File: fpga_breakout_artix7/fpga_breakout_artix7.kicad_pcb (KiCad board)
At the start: 4 copper layers, 26.4 x 25.4 mm, 41 parts, among them U1 XC7A15TCPG236

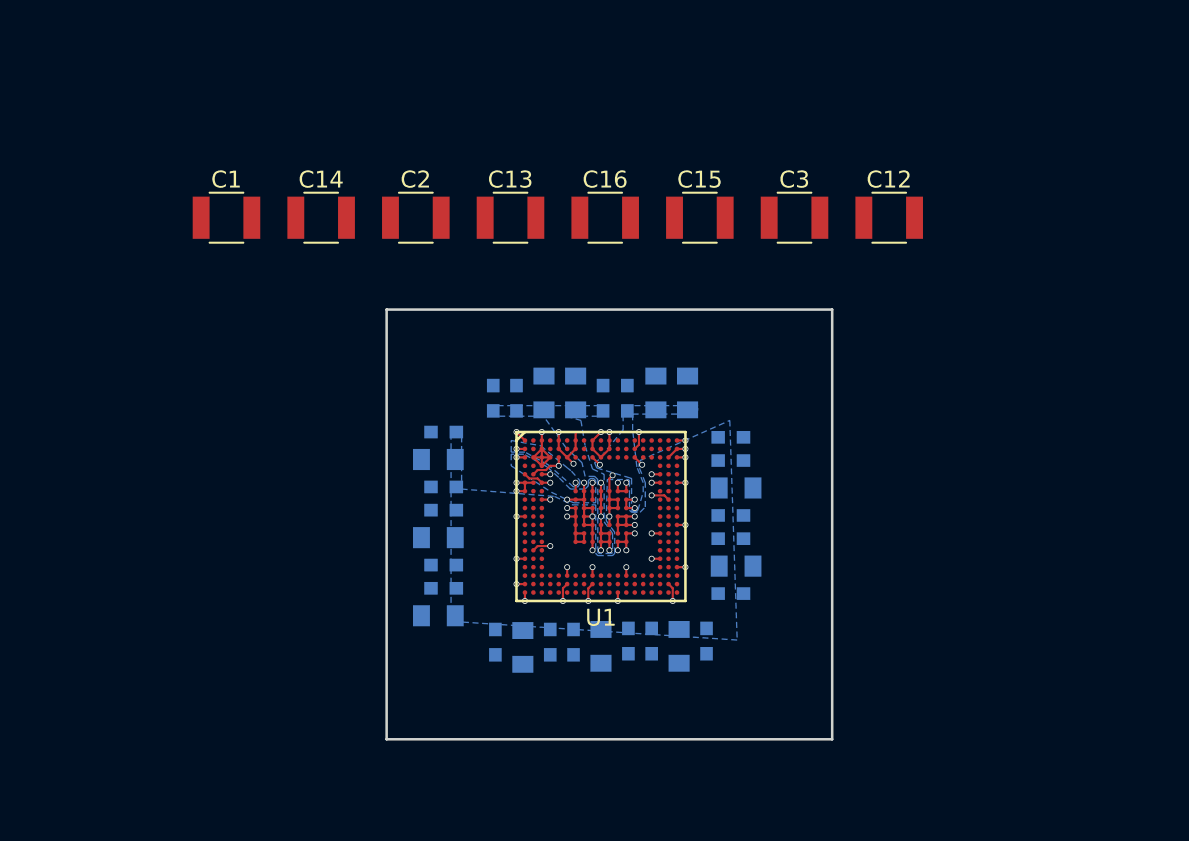
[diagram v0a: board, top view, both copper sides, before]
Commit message: [fpga_breakout_artix7] Added power supply and ufl connectors to schematic.
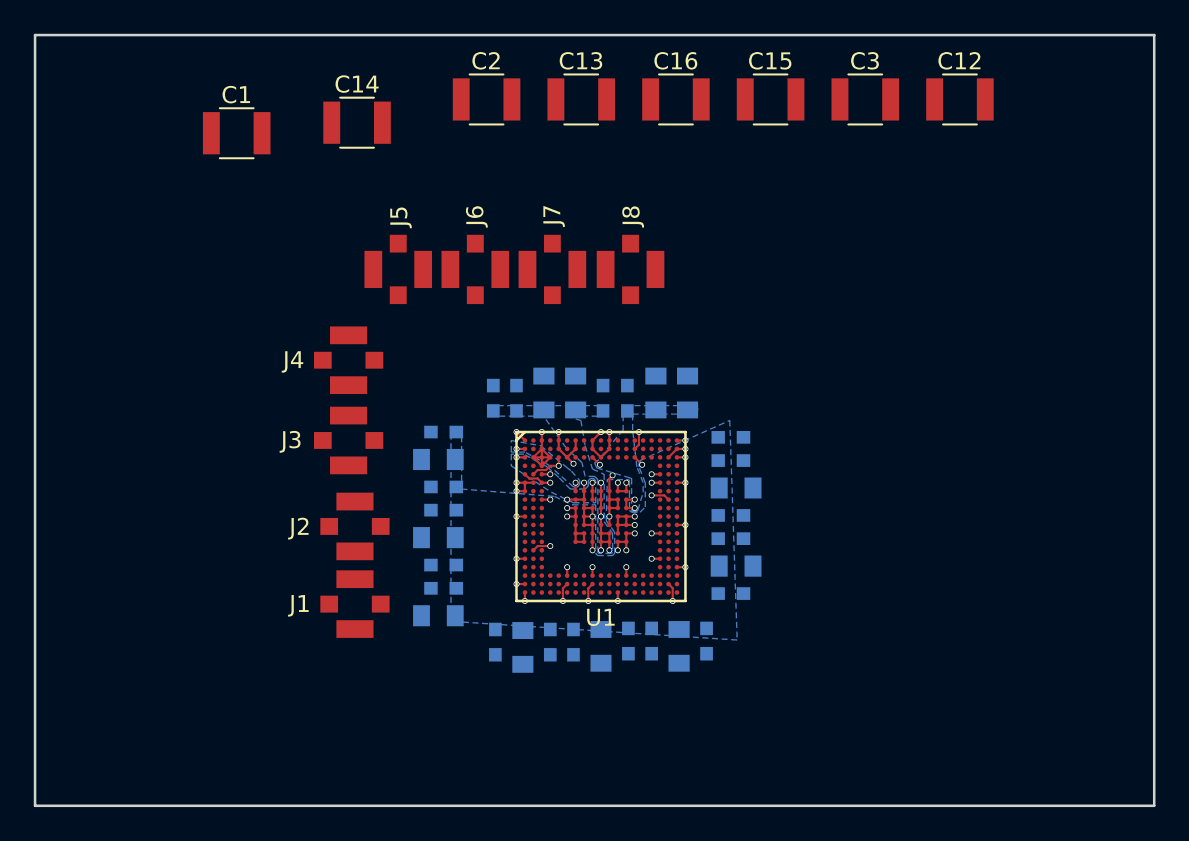
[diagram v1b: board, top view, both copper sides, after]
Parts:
- added J1: CONNECTOR_HS_1x1, NQBit.pretty:UFL_SMA, F.Cu at (131.4, 106.2)
- added J2: CONNECTOR_HS_1x1, NQBit.pretty:UFL_SMA, F.Cu at (131.4, 101.6)
- added J3: CONNECTOR_HS_1x1, NQBit.pretty:UFL_SMA, F.Cu at (131.1, 96.5)
- added J4: CONNECTOR_HS_1x1, NQBit.pretty:UFL_SMA, F.Cu at (131.1, 91.8)
- added J5: CONNECTOR_HS_1x1, NQBit.pretty:UFL_SMA, F.Cu at (134.0, 86.4)
- added J6: CONNECTOR_HS_1x1, NQBit.pretty:UFL_SMA, F.Cu at (138.6, 86.4)
- added J7: CONNECTOR_HS_1x1, NQBit.pretty:UFL_SMA, F.Cu at (143.1, 86.4)
- added J8: CONNECTOR_HS_1x1, NQBit.pretty:UFL_SMA, F.Cu at (147.8, 86.4)
- moved C12 8.16 mm to (167.2, 76.3)
- moved C13 8.16 mm to (144.8, 76.3)
- moved C15 8.16 mm to (156.0, 76.3)
- moved C16 8.16 mm to (150.4, 76.3)
- moved C2 8.16 mm to (139.2, 76.3)
- moved C3 8.16 mm to (161.6, 76.3)
- moved C14 6.01 mm to (131.6, 77.7)
- moved C1 5.04 mm to (124.4, 78.3)
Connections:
- net Net-(U1-PadC8) renamed /JTAG_TCK
- net Net-(U1-PadW10) renamed /JTAG_TDI
- net Net-(U1-PadW8) renamed /JTAG_TDO
- net Net-(U1-PadW9) renamed /JTAG_TMS
- U1 pad A2: Net-(U1-PadA2) -> /GTP1_TX_N
- U1 pad A4: Net-(U1-PadA4) -> /GTP0_RX_N
- U1 pad A6: Net-(U1-PadA6) -> /GTP1_RX_N
- U1 pad B2: Net-(U1-PadB2) -> /GTP1_TX_P
- U1 pad B4: Net-(U1-PadB4) -> /GTP0_RX_P
- U1 pad B6: Net-(U1-PadB6) -> /GTP1_RX_P
- U1 pad D1: Net-(U1-PadD1) -> /GTP0_TX_N
- U1 pad D2: Net-(U1-PadD2) -> /GTP0_TX_P
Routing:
- net GND: track 40.5 -> 40.0 mm
- added copper zone on GND, net GND
- removed copper zone on In2.Cu, net GND
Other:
- board size 26.4 x 25.4 mm -> 66.2 x 45.6 mm
- rule trace_min: 0.127 -> 0.01

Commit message: [fpga_breakout_artix7] Progress on power supply schematic and layout.
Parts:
- added C41: 1uF, Capacitors_SMD:C_0402_NoSilk, F.Cu at (232.5, 127.6)
- added C42: 1uF, Capacitors_SMD:C_0402_NoSilk, F.Cu at (235.2, 128.5)
- added C43: 1uF, Capacitors_SMD:C_0402_NoSilk, F.Cu at (237.9, 126.8)
- added C44: 1uF, Capacitors_SMD:C_0402_NoSilk, F.Cu at (254.2, 134.3)
- added C45: 1uF, Capacitors_SMD:C_0402_NoSilk, F.Cu at (248.7, 133.5)
- added C46: 1uF, Capacitors_SMD:C_0402_NoSilk, F.Cu at (251.5, 131.8)
- added C47: 100nF, Capacitors_SMD:C_0402_NoSilk, F.Cu at (256.9, 132.6)
- added C48: 100nF, Capacitors_SMD:C_0402_NoSilk, F.Cu at (240.6, 131.0)
- added C49: 100nF, Capacitors_SMD:C_0402_NoSilk, F.Cu at (171.8, 86.0)
- added C50: 100nF, Capacitors_SMD:C_0402_NoSilk, F.Cu at (171.8, 87.6)
- added C51: 1uF, Capacitors_SMD:C_0402_NoSilk, F.Cu at (246.0, 129.3)
- added C52: 10uF, Capacitors_SMD:C_0805, F.Cu at (172.8, 156.7)
- added C53: 10uF, Capacitors_SMD:C_0805, F.Cu at (175.5, 157.6)
- added C54: 100uF, Capacitors_SMD:C_0805, F.Cu at (178.2, 155.1)
- added C55: 22uF, Capacitors_SMD:C_0805, F.Cu at (170.0, 158.4)
- added C56: 22uF, Capacitors_SMD:C_0805, F.Cu at (180.9, 155.9)
- added D1: LED, LEDs:LED_0402, F.Cu at (172.1, 96.9)
- added L1: 4.7uH, Inductors:Inductor_Taiyo-Yuden_MD-3030, F.Cu at (158.7, 83.6)
- added L2: 4.7uH, Inductors:Inductor_Taiyo-Yuden_MD-3030, F.Cu at (158.7, 89.5)
- added L3: 2.2uH, NQBit:SRN6045, F.Cu at (178.3, 79.8)
- added L4: 3.3uH, NQBit:SRN4018, F.Cu at (176.3, 93.0)
- added P1: CONN_02X05, Pin_Headers:Pin_Header_Straight_2x05_Pitch1.27mm_SMD, F.Cu at (132.5, 115.0)
- added Q1: MOSFET-N, TO_SOT_Packages_SMD:SOT-23, F.Cu at (145.6, 128.2)
- added Q2: FDS9926A, SMD_Packages:SOIC-8-N, F.Cu at (179.3, 86.7)
- added R1: 100, Resistors_SMD:R_0402_NoSilk, F.Cu at (167.3, 147.7)
- added R10: 1.91k, Resistors_SMD:R_0402_NoSilk, F.Cu at (216.2, 136.8)
- added R11: 31.6k, Resistors_SMD:R_0402_NoSilk, F.Cu at (208.0, 137.6)
- added R12: 4.99k, Resistors_SMD:R_0402_NoSilk, F.Cu at (153.8, 146.0)
- added R13: 0, Resistors_SMD:R_0402_NoSilk, F.Cu at (227.0, 140.1)
- added R14: 0 - DNP, Resistors_SMD:R_0402_NoSilk, F.Cu at (210.8, 139.3)
- added R15: 10.2k, Resistors_SMD:R_0402_NoSilk, F.Cu at (218.9, 142.6)
- added R16: 10.5k, Resistors_SMD:R_0402_NoSilk, F.Cu at (145.6, 143.5)
- added R17: 31.6k, Resistors_SMD:R_0402_NoSilk, F.Cu at (168.2, 80.9)
- added R18: 10.5k, Resistors_SMD:R_0402_NoSilk, F.Cu at (221.6, 141.0)
- added R19: 20k, Resistors_SMD:R_0402_NoSilk, F.Cu at (202.6, 151.8)
- added R2: R, Resistors_SMD:R_0402_NoSilk, F.Cu at (161.9, 146.8)
- added R20: 41.2k, Resistors_SMD:R_0402_NoSilk, F.Cu at (199.9, 151.0)
- added R21: 10.2k, Resistors_SMD:R_0402_NoSilk, F.Cu at (168.4, 79.6)
- added R22: 41.2k, Resistors_SMD:R_0402_NoSilk, F.Cu at (205.3, 138.5)
- added R3: 100k, Resistors_SMD:R_0402_NoSilk, F.Cu at (164.6, 148.5)
- added R4: 0, Resistors_SMD:R_0402_NoSilk, F.Cu at (159.2, 149.3)
- added R5: 301k, Resistors_SMD:R_0402_NoSilk, F.Cu at (191.8, 150.2)
- added R6: 9.53k - DNP, Resistors_SMD:R_0402_NoSilk, F.Cu at (194.5, 152.7)
- added R7: 402k, Resistors_SMD:R_0402_NoSilk, F.Cu at (197.2, 153.5)
- added R8: 47k, Resistors_SMD:R_0402_NoSilk, F.Cu at (213.5, 136.0)
- added R9: 47k, Resistors_SMD:R_0402_NoSilk, F.Cu at (224.3, 141.8)
- added U2: ADP5052, Housings_DFN_QFN:QFN-48-1EP_7x7mm_Pitch0.5mm, F.Cu at (166.4, 86.5)
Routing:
- net /power/BST1: track 0.00 -> 1.52 mm
- net /power/BST2: track 0.00 -> 1.51 mm
- added copper zone on F.Cu, net /power/SW3
- added copper zone on F.Cu, net /power/SW4
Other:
- net class Default: clearance 0.01 -> 0.125
- rule trace_clearance: 0.01 -> 0.125

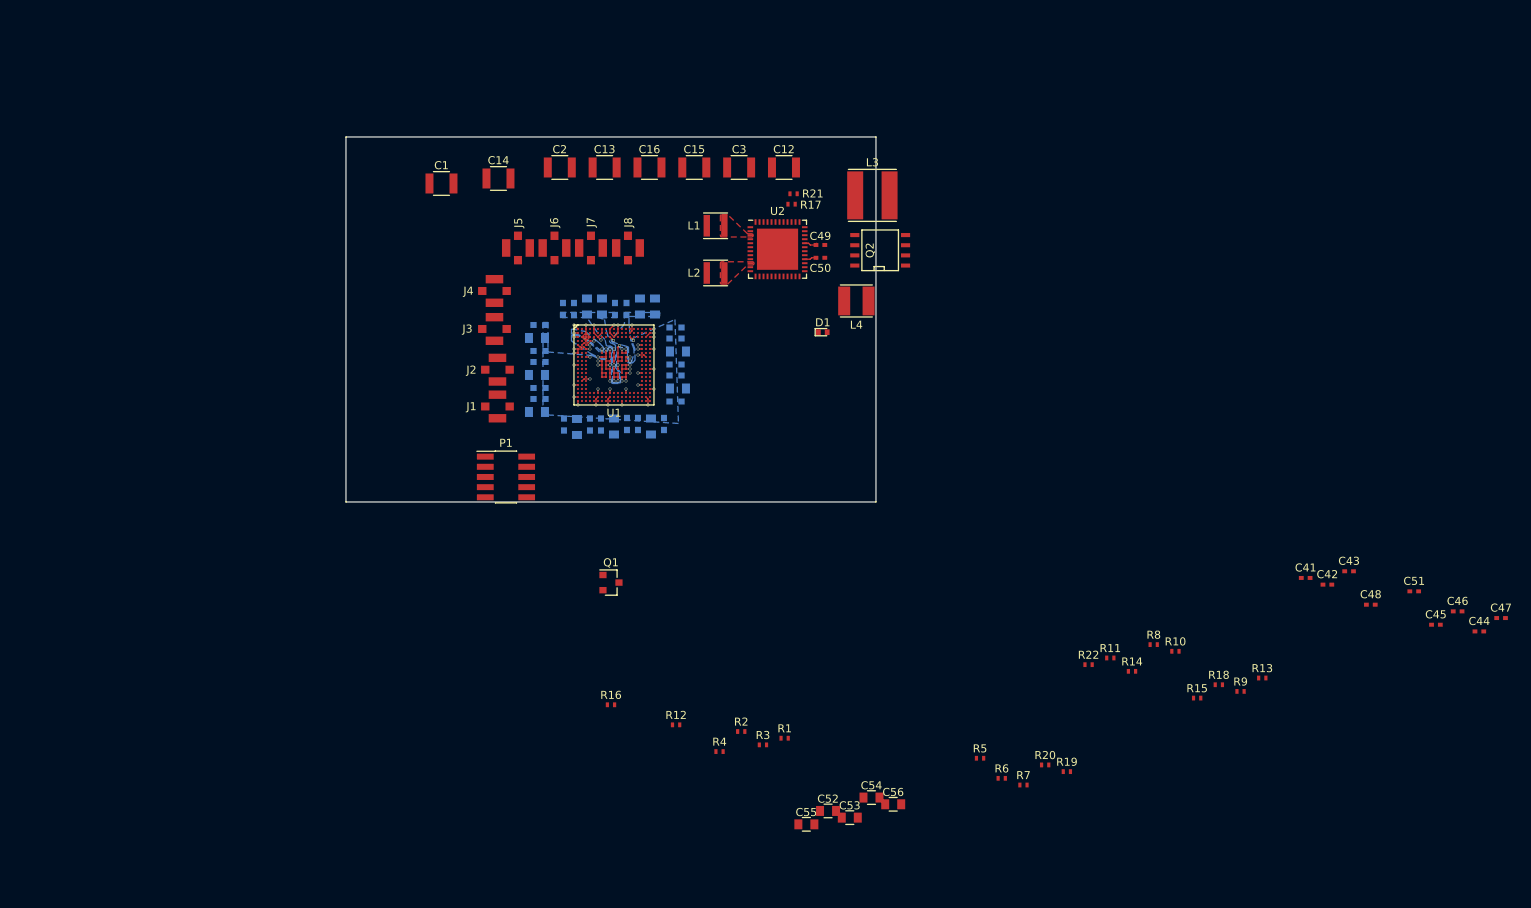
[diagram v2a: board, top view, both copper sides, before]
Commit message: [fpga_breakout_artix7] Added USB-C connector, oscillator, and cleaned up power routing.
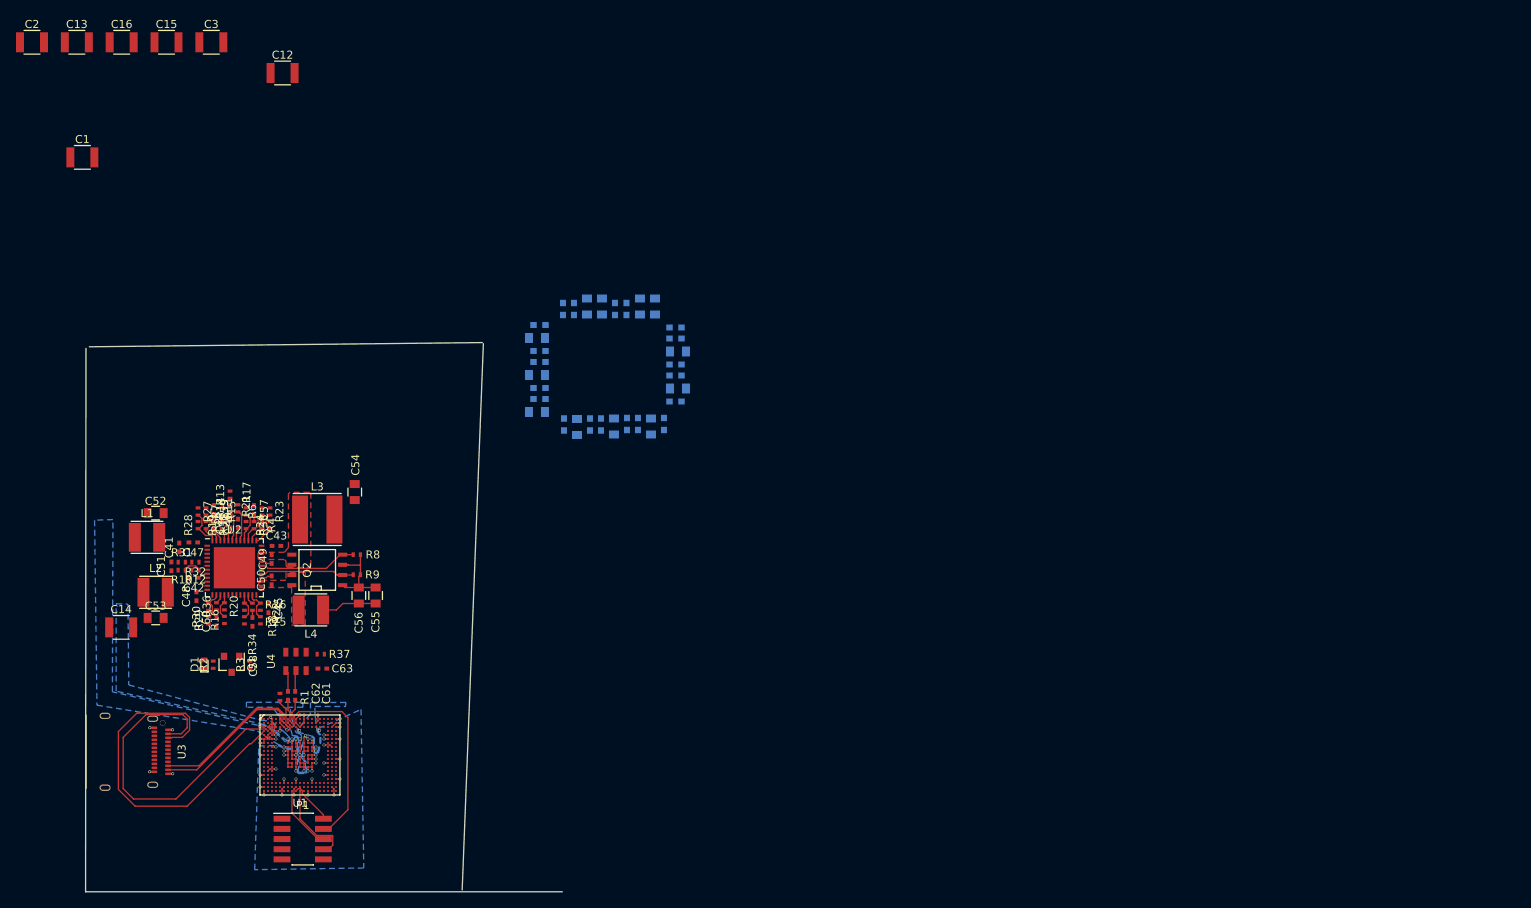
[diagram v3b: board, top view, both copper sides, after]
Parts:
- removed J1, J2, J3, J4, J5, J6, J7, J8: CONNECTOR_HS_1x1, NQBit.pretty:UFL_SMA
- added C57: 2.7nF, Capacitors_SMD:C_0402_NoSilk, F.Cu at (101.0, 119.1)
- added C58: 2.7nF, Capacitors_SMD:C_0402_NoSilk, F.Cu at (100.8, 133.1)
- added C59: 2.7nF, Capacitors_SMD:C_0402_NoSilk, F.Cu at (96.0, 119.1)
- added C60: 2.7nF, Capacitors_SMD:C_0402_NoSilk, F.Cu at (96.3, 133.1)
- added C61: 100nF, Capacitors_SMD:C_0402_NoSilk, F.Cu at (106.2, 142.3)
- added C62: 100nF, Capacitors_SMD:C_0402_NoSilk, F.Cu at (105.2, 142.3)
- added C63: 100nF, Capacitors_SMD:C_0402_NoSilk, F.Cu at (109.5, 138.9)
- added R23: 56.2k, Resistors_SMD:R_0402_NoSilk, F.Cu at (103.0, 119.3)
- added R24: 56.2k, Resistors_SMD:R_0402_NoSilk, F.Cu at (103.0, 121.0)
- added R25: 56.2k, Resistors_SMD:R_0402_NoSilk, F.Cu at (101.8, 132.9)
- added R26: 56.2k, Resistors_SMD:R_0402_NoSilk, F.Cu at (101.8, 131.2)
- added R27: 56.2k, Resistors_SMD:R_0402_NoSilk, F.Cu at (94.0, 119.3)
- added R28: 56.2k, Resistors_SMD:R_0402_NoSilk, F.Cu at (94.0, 121.0)
- added R29: 56.2k, Resistors_SMD:R_0402_NoSilk, F.Cu at (95.3, 132.9)
- added R30: 56.2k, Resistors_SMD:R_0402_NoSilk, F.Cu at (95.3, 131.2)
- added R31: 56.2k, Resistors_SMD:R_0402_NoSilk, F.Cu at (92.0, 125.6)
- added R32: 56.2k, Resistors_SMD:R_0402_NoSilk, F.Cu at (93.7, 125.6)
- added R33: 56.2k, Resistors_SMD:R_0402_NoSilk, F.Cu at (101.0, 121.0)
- added R34: 56.2k, Resistors_SMD:R_0402_NoSilk, F.Cu at (100.8, 131.2)
- added R35: 56.2k, Resistors_SMD:R_0402_NoSilk, F.Cu at (96.0, 121.0)
- added R36: 56.2k, Resistors_SMD:R_0402_NoSilk, F.Cu at (96.3, 131.2)
- added R37: 10k, Resistors_SMD:R_0402_NoSilk, F.Cu at (109.3, 137.2)
- added U3: USB-C, NQBit:USB-C_SMT, F.Cu at (89.6, 149.3)
- added U4: DSC1123, NQBit:DSC1123, F.Cu at (106.2, 138.1)
- L1, L2: footprint Inductors:Inductor_Taiyo-Yuden_MD-3030 -> NQBit:SRN4018
- R15: value 10.2k -> 10.5k
- R16: value 10.5k -> 10.2k
- R19: value 20k -> 41.2k
- R2: value R -> 4.7k
- R20: value 41.2k -> 20k
- moved C47 163.7 mm to (93.4, 123.2), turned to 180 degrees
- moved C44 156.7 mm to (98.0, 120.8), turned to 90 degrees
- moved C51 155.4 mm to (90.7, 126.2), turned to 90 degrees
- moved C46 152.8 mm to (99.0, 120.8), turned to 90 degrees
- moved C48 146.8 mm to (93.8, 129.9), turned to 90 degrees
- moved C45 146.0 mm to (102.8, 131.4), turned to 270 degrees
- moved C42 141.7 mm to (93.5, 127.6), turned to 180 degrees
- moved C41 140.9 mm to (91.7, 123.8), turned to 90 degrees
- moved C43 134.1 mm to (103.8, 123.6)
- moved R13 131.0 mm to (98.0, 117.2), turned to 90 degrees
- moved R10 124.6 mm to (92.0, 126.6), turned to 180 degrees
- moved R15 124.1 mm to (97.0, 119.3), turned to 270 degrees
- moved R18 122.1 mm to (99.8, 132.9), turned to 90 degrees
- moved R14 114.6 mm to (98.0, 118.9), turned to 90 degrees
- moved R9 111.4 mm to (113.9, 127.2), turned to 180 degrees
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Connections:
- C52 pad 1: /power/AVCC1V2 -> /power/AVCC1V0
- C53 pad 1: /power/AVCC1V0 -> /power/AVCC1V2
- L1 pad 2: /power/AVCC1V2 -> /power/AVCC1V0
- L2 pad 2: /power/AVCC1V0 -> /power/AVCC1V2
- P1 pad 10: /RESET -> (no net)
- P1 pad 7: Net-(P1-Pad7) -> (no net)
- R15 pad 1: /power/AVCC1V2 -> /power/AVCC1V0
- R16 pad 1: /power/AVCC1V0 -> /power/AVCC1V2
- U1 pad A10: Net-(U1-PadA10) -> (no net)
- U1 pad A12: Net-(U1-PadA12) -> (no net)
- U1 pad A13: Net-(U1-PadA13) -> (no net)
- U1 pad A14: Net-(U1-PadA14) -> (no net)
- U1 pad A15: Net-(U1-PadA15) -> (no net)
- U1 pad A16: Net-(U1-PadA16) -> (no net)
- U1 pad A17: Net-(U1-PadA17) -> (no net)
- U1 pad A8: Net-(U1-PadA8) -> /GTP_REF_CLK_N
- U1 pad B10: Net-(U1-PadB10) -> (no net)
- U1 pad B12: Net-(U1-PadB12) -> (no net)
- U1 pad B13: Net-(U1-PadB13) -> (no net)
- U1 pad B15: Net-(U1-PadB15) -> (no net)
- U1 pad B16: Net-(U1-PadB16) -> (no net)
- U1 pad B17: Net-(U1-PadB17) -> (no net)
- U1 pad B8: Net-(U1-PadB8) -> /GTP_REF_CLK_P
- U1 pad C11: Net-(U1-PadC11) -> (no net)
- U1 pad C12: Net-(U1-PadC12) -> (no net)
- U1 pad C13: Net-(U1-PadC13) -> (no net)
- U1 pad C15: Net-(U1-PadC15) -> (no net)
- U1 pad C16: Net-(U1-PadC16) -> (no net)
- U1 pad C17: Net-(U1-PadC17) -> (no net)
- U1 pad D17: Net-(U1-PadD17) -> (no net)
- U1 pad D18: Net-(U1-PadD18) -> (no net)
- U1 pad D19: Net-(U1-PadD19) -> (no net)
- U1 pad E18: Net-(U1-PadE18) -> (no net)
- U1 pad E19: Net-(U1-PadE19) -> (no net)
- U1 pad F18: Net-(U1-PadF18) -> (no net)
- U1 pad G17: Net-(U1-PadG17) -> (no net)
- U1 pad G18: Net-(U1-PadG18) -> (no net)
- U1 pad G19: Net-(U1-PadG19) -> (no net)
- U1 pad G2: Net-(U1-PadG2) -> (no net)
- U1 pad G3: Net-(U1-PadG3) -> (no net)
- U1 pad H1: Net-(U1-PadH1) -> (no net)
- U1 pad H17: Net-(U1-PadH17) -> (no net)
- U1 pad H19: Net-(U1-PadH19) -> (no net)
- U1 pad H2: Net-(U1-PadH2) -> (no net)
- U1 pad J1: Net-(U1-PadJ1) -> (no net)
- U1 pad J17: Net-(U1-PadJ17) -> (no net)
- U1 pad J18: Net-(U1-PadJ18) -> (no net)
- U1 pad J19: Net-(U1-PadJ19) -> (no net)
- U1 pad J2: Net-(U1-PadJ2) -> (no net)
- U1 pad J3: Net-(U1-PadJ3) -> (no net)
- U1 pad K17: Net-(U1-PadK17) -> (no net)
- U1 pad K18: Net-(U1-PadK18) -> (no net)
- U1 pad K19: Net-(U1-PadK19) -> (no net)
- U1 pad K2: Net-(U1-PadK2) -> (no net)
- U1 pad K3: Net-(U1-PadK3) -> (no net)
- U1 pad L1: Net-(U1-PadL1) -> (no net)
- U1 pad L17: Net-(U1-PadL17) -> (no net)
- U1 pad L18: Net-(U1-PadL18) -> (no net)
- U1 pad L2: Net-(U1-PadL2) -> (no net)
- U1 pad L3: Net-(U1-PadL3) -> (no net)
- U1 pad M1: Net-(U1-PadM1) -> (no net)
- U1 pad M18: Net-(U1-PadM18) -> (no net)
- U1 pad M19: Net-(U1-PadM19) -> (no net)
- U1 pad M2: Net-(U1-PadM2) -> (no net)
- U1 pad M3: Net-(U1-PadM3) -> (no net)
- U1 pad N1: Net-(U1-PadN1) -> (no net)
- U1 pad N17: Net-(U1-PadN17) -> (no net)
- U1 pad N18: Net-(U1-PadN18) -> (no net)
- U1 pad N19: Net-(U1-PadN19) -> (no net)
- U1 pad N2: Net-(U1-PadN2) -> (no net)
- U1 pad N3: Net-(U1-PadN3) -> (no net)
- U1 pad P1: Net-(U1-PadP1) -> (no net)
- U1 pad P17: Net-(U1-PadP17) -> (no net)
- U1 pad P18: Net-(U1-PadP18) -> (no net)
- U1 pad P19: Net-(U1-PadP19) -> (no net)
- U1 pad P3: Net-(U1-PadP3) -> (no net)
- U1 pad R18: Net-(U1-PadR18) -> (no net)
- U1 pad R19: Net-(U1-PadR19) -> (no net)
- U1 pad R2: Net-(U1-PadR2) -> (no net)
- U1 pad R3: Net-(U1-PadR3) -> (no net)
- U1 pad T1: Net-(U1-PadT1) -> (no net)
- U1 pad T17: Net-(U1-PadT17) -> (no net)
- U1 pad T18: Net-(U1-PadT18) -> (no net)
- U1 pad T2: Net-(U1-PadT2) -> (no net)
- U1 pad T3: Net-(U1-PadT3) -> (no net)
- U1 pad U1: Net-(U1-PadU1) -> (no net)
- U1 pad U10: Net-(U1-PadU10) -> (no net)
- U1 pad U11: Net-(U1-PadU11) -> (no net)
- U1 pad U12: Net-(U1-PadU12) -> (no net)
- U1 pad U14: Net-(U1-PadU14) -> (no net)
- U1 pad U15: Net-(U1-PadU15) -> (no net)
- U1 pad U16: Net-(U1-PadU16) -> (no net)
- U1 pad U17: Net-(U1-PadU17) -> (no net)
- U1 pad U18: Net-(U1-PadU18) -> (no net)
- U1 pad U19: Net-(U1-PadU19) -> (no net)
- U1 pad U2: Net-(U1-PadU2) -> (no net)
- U1 pad U3: Net-(U1-PadU3) -> (no net)
- U1 pad U4: Net-(U1-PadU4) -> (no net)
- U1 pad U5: Net-(U1-PadU5) -> (no net)
- U1 pad U7: Net-(U1-PadU7) -> (no net)
- U1 pad U8: Net-(U1-PadU8) -> (no net)
- U1 pad V10: Net-(U1-PadV10) -> (no net)
- U1 pad V11: Net-(U1-PadV11) -> (no net)
- U1 pad V12: Net-(U1-PadV12) -> (no net)
- U1 pad V13: Net-(U1-PadV13) -> (no net)
- U1 pad V14: Net-(U1-PadV14) -> (no net)
- U1 pad V15: Net-(U1-PadV15) -> (no net)
- U1 pad V16: Net-(U1-PadV16) -> (no net)
- U1 pad V17: Net-(U1-PadV17) -> (no net)
- U1 pad V19: Net-(U1-PadV19) -> (no net)
- U1 pad V2: Net-(U1-PadV2) -> (no net)
- U1 pad V3: Net-(U1-PadV3) -> (no net)
- U1 pad V4: Net-(U1-PadV4) -> (no net)
- U1 pad V5: Net-(U1-PadV5) -> (no net)
- U1 pad V7: Net-(U1-PadV7) -> (no net)
- U1 pad V8: Net-(U1-PadV8) -> (no net)
- U1 pad W11: Net-(U1-PadW11) -> (no net)
- U1 pad W13: Net-(U1-PadW13) -> (no net)
- U1 pad W14: Net-(U1-PadW14) -> (no net)
- U1 pad W15: Net-(U1-PadW15) -> (no net)
- U1 pad W16: Net-(U1-PadW16) -> (no net)
- U1 pad W17: Net-(U1-PadW17) -> (no net)
- U1 pad W18: Net-(U1-PadW18) -> (no net)
- U1 pad W19: Net-(U1-PadW19) -> (no net)
- U1 pad W2: Net-(U1-PadW2) -> (no net)
- U1 pad W3: Net-(U1-PadW3) -> (no net)
- U1 pad W4: Net-(U1-PadW4) -> (no net)
- U1 pad W5: Net-(U1-PadW5) -> (no net)
- U1 pad W6: Net-(U1-PadW6) -> (no net)
- U1 pad W7: Net-(U1-PadW7) -> (no net)
- U2 pad 11: Net-(U2-Pad11) -> GND
- U2 pad 13: Net-(U2-Pad13) -> GND
- U2 pad 17: Net-(U2-Pad17) -> GND
- U2 pad 18: Net-(U2-Pad18) -> GND
- U2 pad 19: Net-(U2-Pad19) -> GND
- U2 pad 2: Net-(U2-Pad2) -> GND
- U2 pad 30: Net-(U2-Pad30) -> GND
- U2 pad 49: Net-(U2-Pad49) -> GND
- U2 pad 5: Net-(U2-Pad5) -> /power/EN5
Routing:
- net /GTP0_TX_N: track 0.00 -> 44.9 mm
- net /GTP0_TX_P: track 0.00 -> 42.0 mm
- net /JTAG_TCK: track 0.00 -> 24.3 mm
- net /GTP1_RX_P: track 0.00 -> 18.8 mm
- net /GTP1_RX_N: track 0.00 -> 18.4 mm
- net GND: track 40.0 -> 53.3 mm, vias 32 -> 36
- net /power/DL1: track 0.00 -> 12.3 mm
- net /power/DL2: track 0.00 -> 11.8 mm
- net /JTAG_TDI: track 0.00 -> 11.0 mm
- net /JTAG_TDO: track 0.00 -> 8.03 mm
- net /power/VCC1V0: track 0.00 -> 6.91 mm
- net /JTAG_TMS: track 0.00 -> 5.61 mm
- net /power/EN3: track 0.00 -> 4.89 mm
- net /power/SS34: track 0.00 -> 4.62 mm
- net /power/EN1: track 0.00 -> 4.56 mm
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- added copper zone on F.Cu, net /power/SW1
- added copper zone on F.Cu, net /power/SW2
- removed copper zone on F.Cu, net /power/SW3
- removed copper zone on F.Cu, net /power/SW4
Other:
- board size 66.2 x 45.6 mm -> 59.6 x 68.6 mm
- net class Default: clearance 0.125 -> 0.057; trace_width 0.127 -> 0.125
- net class Highspeed added: clearance 0.057, trace_width 0.1143, via_dia 0.354, via_drill 0.254
- rule trace_clearance: 0.125 -> 0.057
